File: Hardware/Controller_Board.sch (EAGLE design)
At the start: 49 parts, among them K1 E3206S, K2 E3206S, K3 E3206S, K4 E3206S, K5 E3206S, K6 E3206S, Q1 BD135, Q2 BD135, Q3 BD135, Q4 BD135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

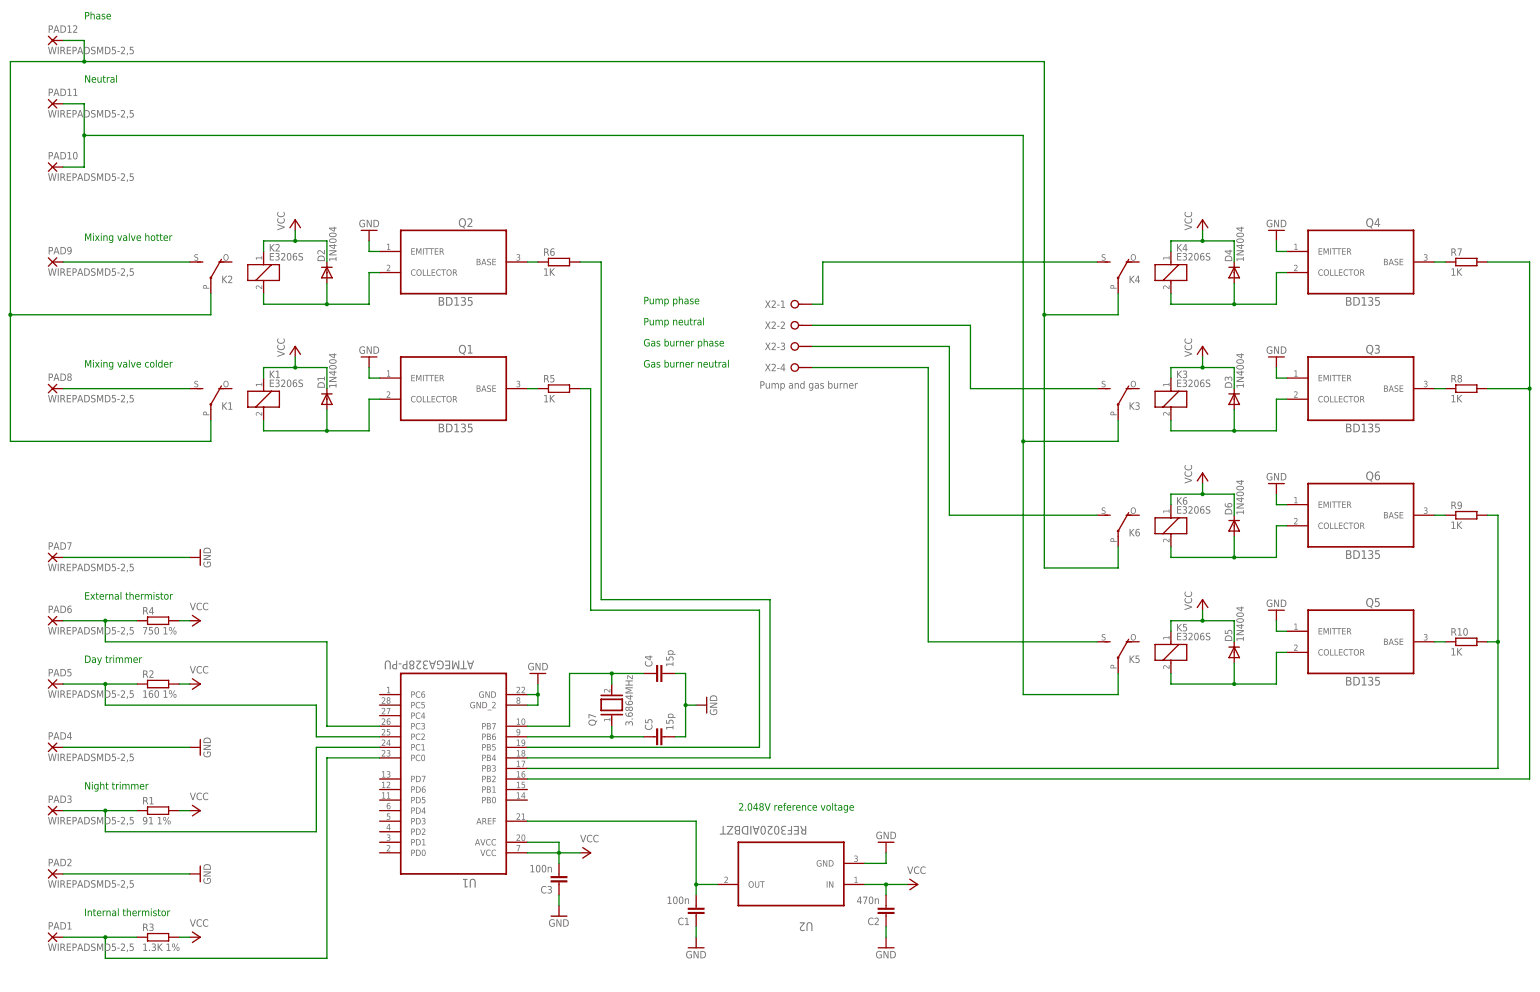
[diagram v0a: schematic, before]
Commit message: Splitted circuit in two PCBs to ease routing.
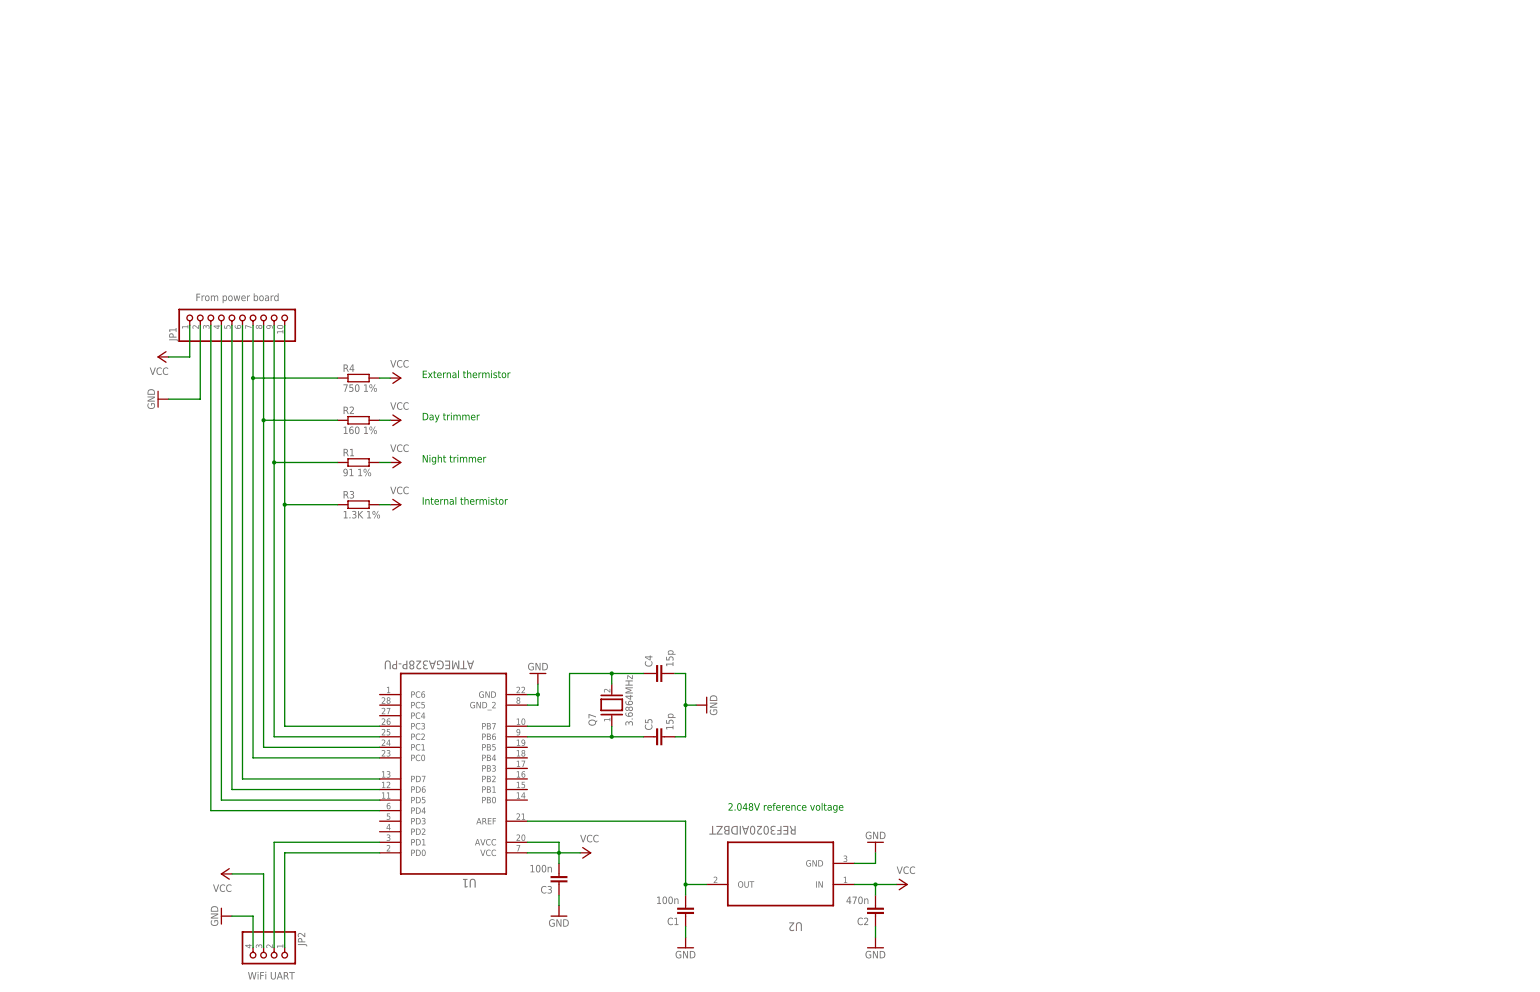
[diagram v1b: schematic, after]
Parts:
- removed D1, D2, D3, D4, D5, D6: 1N4004, diode:1N4004
- removed K1, K2, K3, K4, K5, K6: E3206S, relay:E3206S
- removed PAD1, PAD10, PAD11, PAD12, PAD2, PAD3, PAD4, PAD5, PAD6, PAD7, PAD8, PAD9: WIREPADSMD5-2,5, wirepad:WIREPADSMD5-2,5
- removed Q1, Q2, Q3, Q4, Q5, Q6: BD135, BD135:BD135
- removed R10, R5, R6, R7, R8, R9: 1K, resistor:R-EU_0207/10
- removed X2: Pump and gas burner, con-wago-508:W237-04P
- added JP1: From power board, pinhead:PINHD-1X10
- added JP2: WiFi UART, pinhead:PINHD-1X4
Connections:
- removed net N$11: K52.S, X2-4.KL
- removed net N$12: K32.S, X2-2.KL
- removed net N$13: D3.A, K31.2, Q3.COLLECTOR
- removed net N$14: K42.S, X2-1.KL
- removed net N$15: D4.A, K41.2, Q4.COLLECTOR
- removed net N$17: D5.A, K51.2, Q5.COLLECTOR
- removed net N$18: K62.S, X2-3.KL
- removed net N$19: D6.A, K61.2, Q6.COLLECTOR
- removed net N$20: Q2.BASE, R6.1
- removed net N$21: R5.2, U1.PB5
- removed net N$22: R6.2, U1.PB4
- removed net N$23: R10.2, R9.2, U1.PB3
- removed net N$24: Q5.BASE, R10.1
- removed net N$25: Q6.BASE, R9.1
- removed net N$26: R7.2, R8.2, U1.PB2
- removed net N$28: Q3.BASE, R8.1
- removed net N$31: K32.P, K52.P, PAD10.P, PAD11.P
- removed net PIN4: PAD3.P, R1.1, U1.PC1
- net GND: now also JP1.2, JP2.4; no longer PAD2.P, PAD4.P, PAD7.P, Q1.EMITTER, Q2.EMITTER, Q3.EMITTER, Q4.EMITTER, Q5.EMITTER, Q6.EMITTER
- net N$1: now also JP1.10, R3.1, U1.PC3; no longer PAD5.P, R2.1, U1.PC2
- net N$10: now also JP2.1, U1.PD0; no longer K12.P, K22.P, K42.P, K62.P, PAD12.P
- net N$2: now also JP1.9, R1.1, U1.PC2; no longer PAD1.P, R3.1, U1.PC0
- net N$3: now also JP1.8, R2.1, U1.PC1; no longer K12.S, PAD8.P
- net N$4: now also JP1.7, R4.1, U1.PC0; no longer D1.A, K11.2, Q1.COLLECTOR
- net N$5: now also JP1.6, U1.PD7; no longer Q4.BASE, R7.1
- net N$6: now also JP1.5, U1.PD6; no longer K22.S, PAD9.P
- net N$7: now also JP1.4, U1.PD5; no longer D2.A, K21.2, Q2.COLLECTOR
- net N$8: now also JP1.3, U1.PD4; no longer PAD6.P, R4.1, U1.PC3
- net N$9: now also JP2.2, U1.PD1; no longer Q1.BASE, R5.1
- net VCC: now also JP1.1, JP2.3; no longer D1.C, D2.C, D3.C, D4.C, D5.C, D6.C, K11.1, K21.1, K31.1, K41.1, K51.1, K61.1
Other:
- note removed: "Gas burner neutral"
- note removed: "Gas burner phase"
- note removed: "Mixing valve colder"
- note removed: "Mixing valve hotter"
- note removed: "Neutral"
- note removed: "Phase"
- note removed: "Pump neutral"
- note removed: "Pump phase"
- moved on the sheet: C1, C2, R1, R2, R3, R4, U2
